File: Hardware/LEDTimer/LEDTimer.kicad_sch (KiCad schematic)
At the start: 36 parts, among them J2 LED, J3 PWR_IN, SW1 SW_Push, SW2 SW_Push, SW3 SW_Push, SW4 SW_BAT, U1 AP7383-36WW7, U2 PIC16F1825, U3 Display_128x64_096_I2C, U4 BCR_421U_E6327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

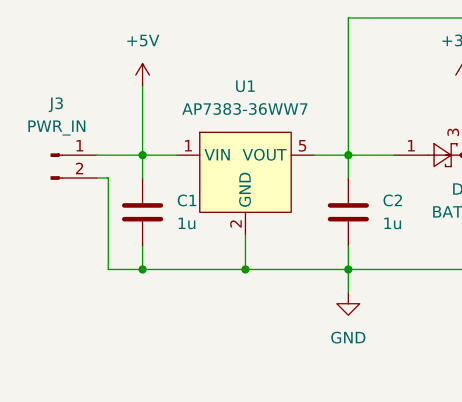
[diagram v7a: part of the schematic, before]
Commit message: PCB: fix DRC issues
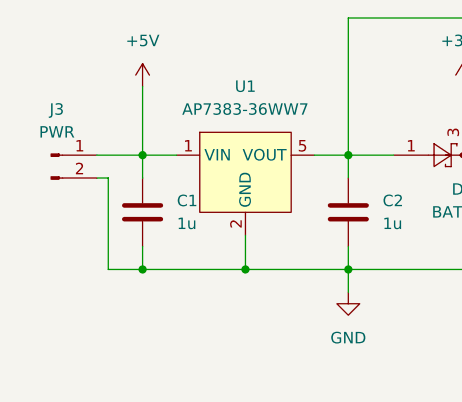
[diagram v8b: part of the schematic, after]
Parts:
- J3: value PWR_IN -> PWR
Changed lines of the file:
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@@
   (symbol (lib_id "Connector:Conn_01x02_Male") (at 20.32 41.91 0) (unit 1)
     (in_bom yes) (on_board yes) (fields_autoplaced)
-    (property "Reference" "J3" (id 0) (at 20.955 36.195 0))
-    (property "Value" "PWR_IN" (id 1) (at 20.955 38.735 0))
+    (property "Reference" "J3" (id 0) (at 20.955 36.83 0))
+    (property "Value" "PWR" (id 1) (at 20.955 39.37 0))
     (property "Footprint" "Connector_PinHeader_2.54mm:PinHeader_1x02_P2.54mm_Horizontal" (id 2) (at 20.32 41.91 0)
       (effects (font (size 1.27 1.27)) hide)
@@
     )
     (path "/5fea63b6-f6d3-4655-9ba8-29ebbdc154a7"
-      (reference "J3") (unit 1) (value "PWR_IN") (footprint "Connector_PinHeader_2.54mm:PinHeader_1x02_P2.54mm_Horizontal")
+      (reference "J3") (unit 1) (value "PWR") (footprint "Connector_PinHeader_2.54mm:PinHeader_1x02_P2.54mm_Horizontal")
     )
     (path "/ca50989c-806e-4138-b3ff-f2b2f96652a0"
